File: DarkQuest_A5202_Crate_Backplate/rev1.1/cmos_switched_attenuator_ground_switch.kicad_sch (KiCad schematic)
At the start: 9 parts, among them U17 TMUX7612RUMR

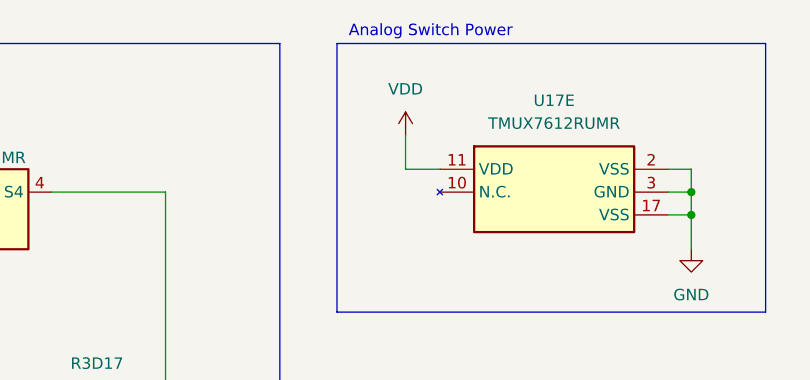
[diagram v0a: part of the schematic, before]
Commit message: Update DR, resolve all DRC except 2-pin routing
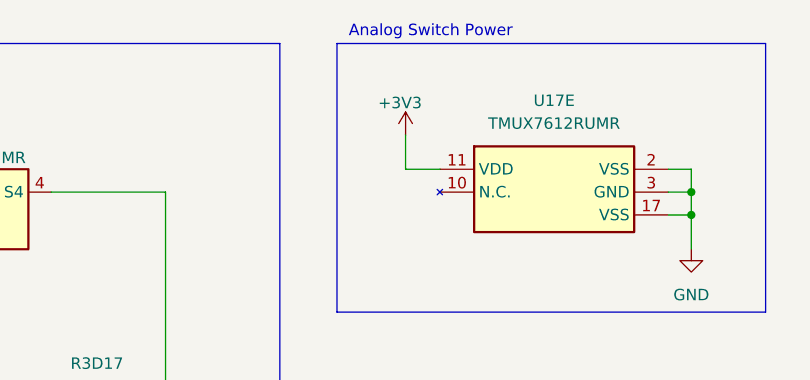
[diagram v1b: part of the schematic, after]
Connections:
- net VDD renamed +3V3
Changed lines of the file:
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@@
 		(on_board yes)
 		(dnp no)
-		(fields_autoplaced yes)
 		(property "Reference" "#PWR072"
 			(at 204.47 45.72 0)
@@
 			)
 		)
-		(property "Value" "VDD"
-			(at 204.47 36.83 0)
+		(property "Value" "+3V3"
+			(at 201.422 38.354 0)
 			(effects
 				(font
 					(size 1.27 1.27)
 				)
+				(justify left)
 			)
 		)

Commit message: Fix net class widths, refdes numbering
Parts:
- renumbered C34 to C3A2, C35 to C3B2, R3A17 to R3A18, R3B17 to R3B18, R3C17 to R3C18, R3D17 to R3D18, R4A17 to R4A18, R4B17 to R4B18, U17 to U18
